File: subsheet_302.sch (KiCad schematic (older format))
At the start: 14 parts, among them J302 Internal FDD Power, J303 Internal FDD Port, J304 DIN-14S — External FDD Port, U301 WD1772_FLOPPY_DISK_CONTROLLER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, U305 7406_PHY

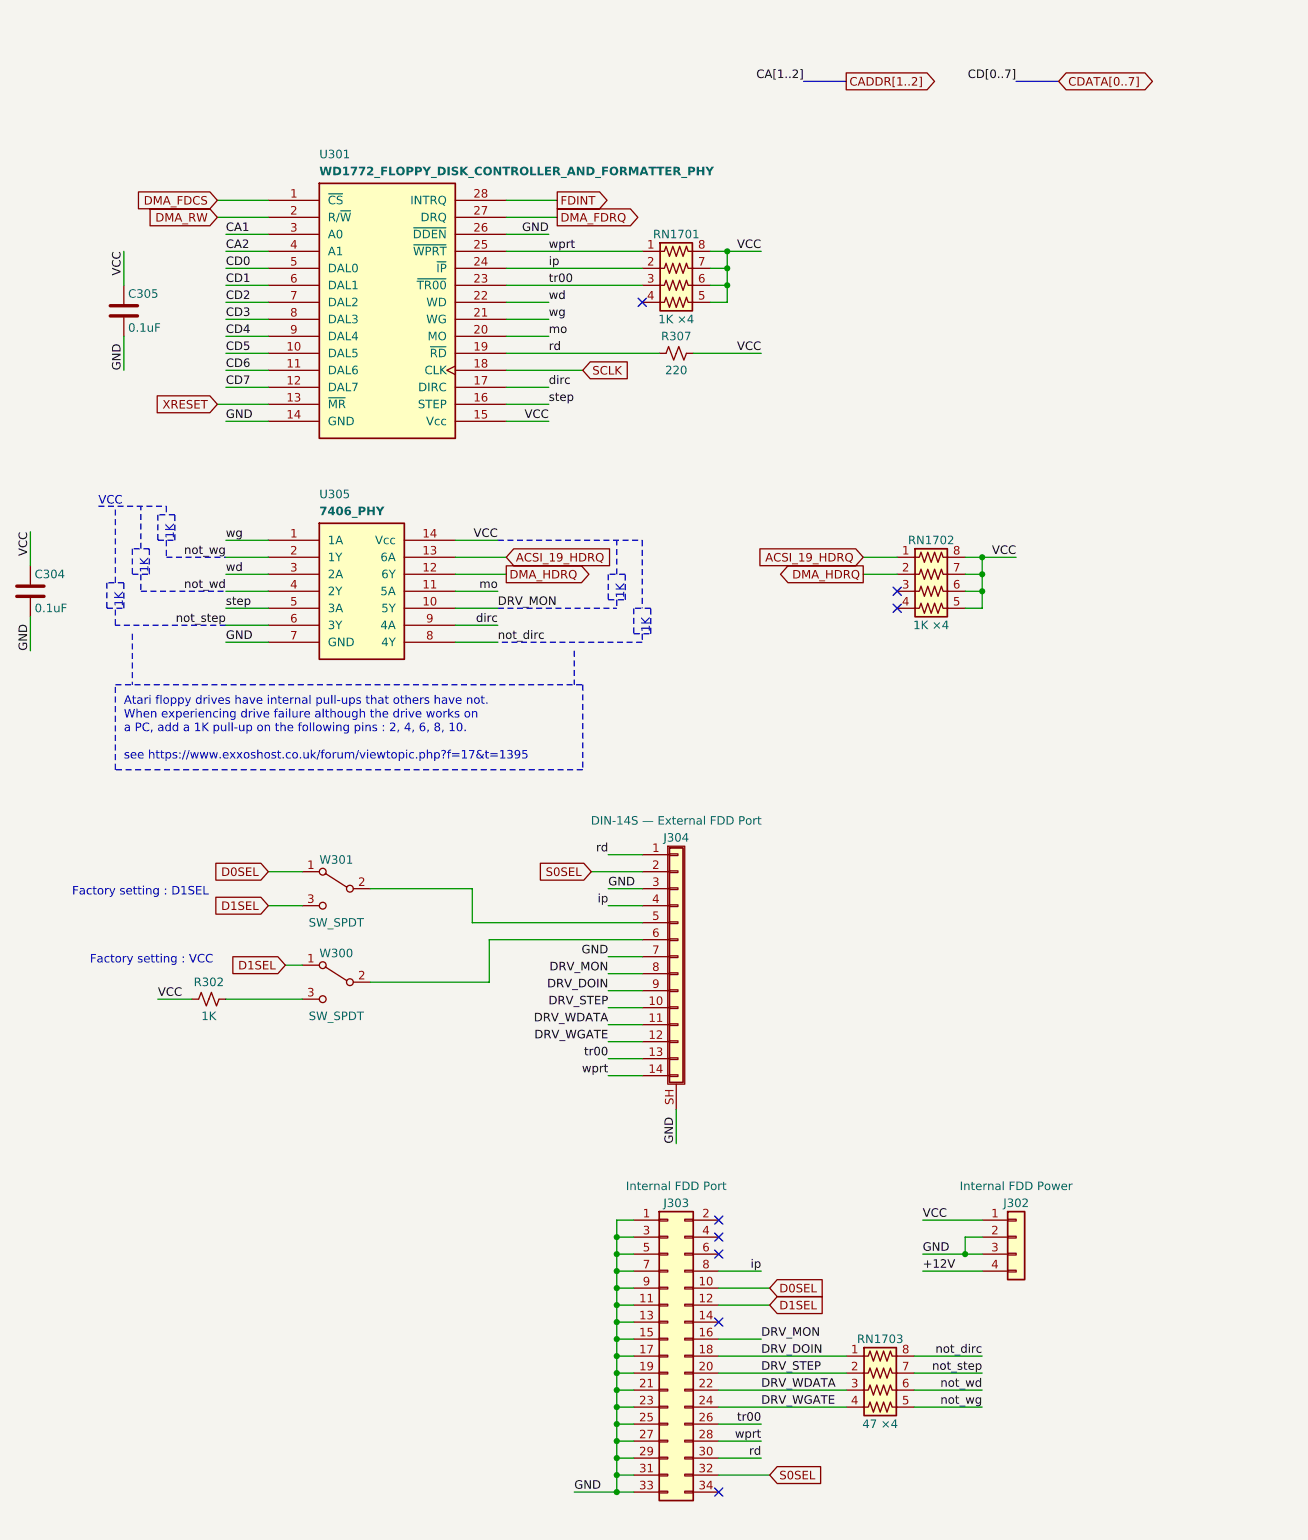
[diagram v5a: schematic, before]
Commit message: Resolves #4 : Apply the 1772 pull-up fix
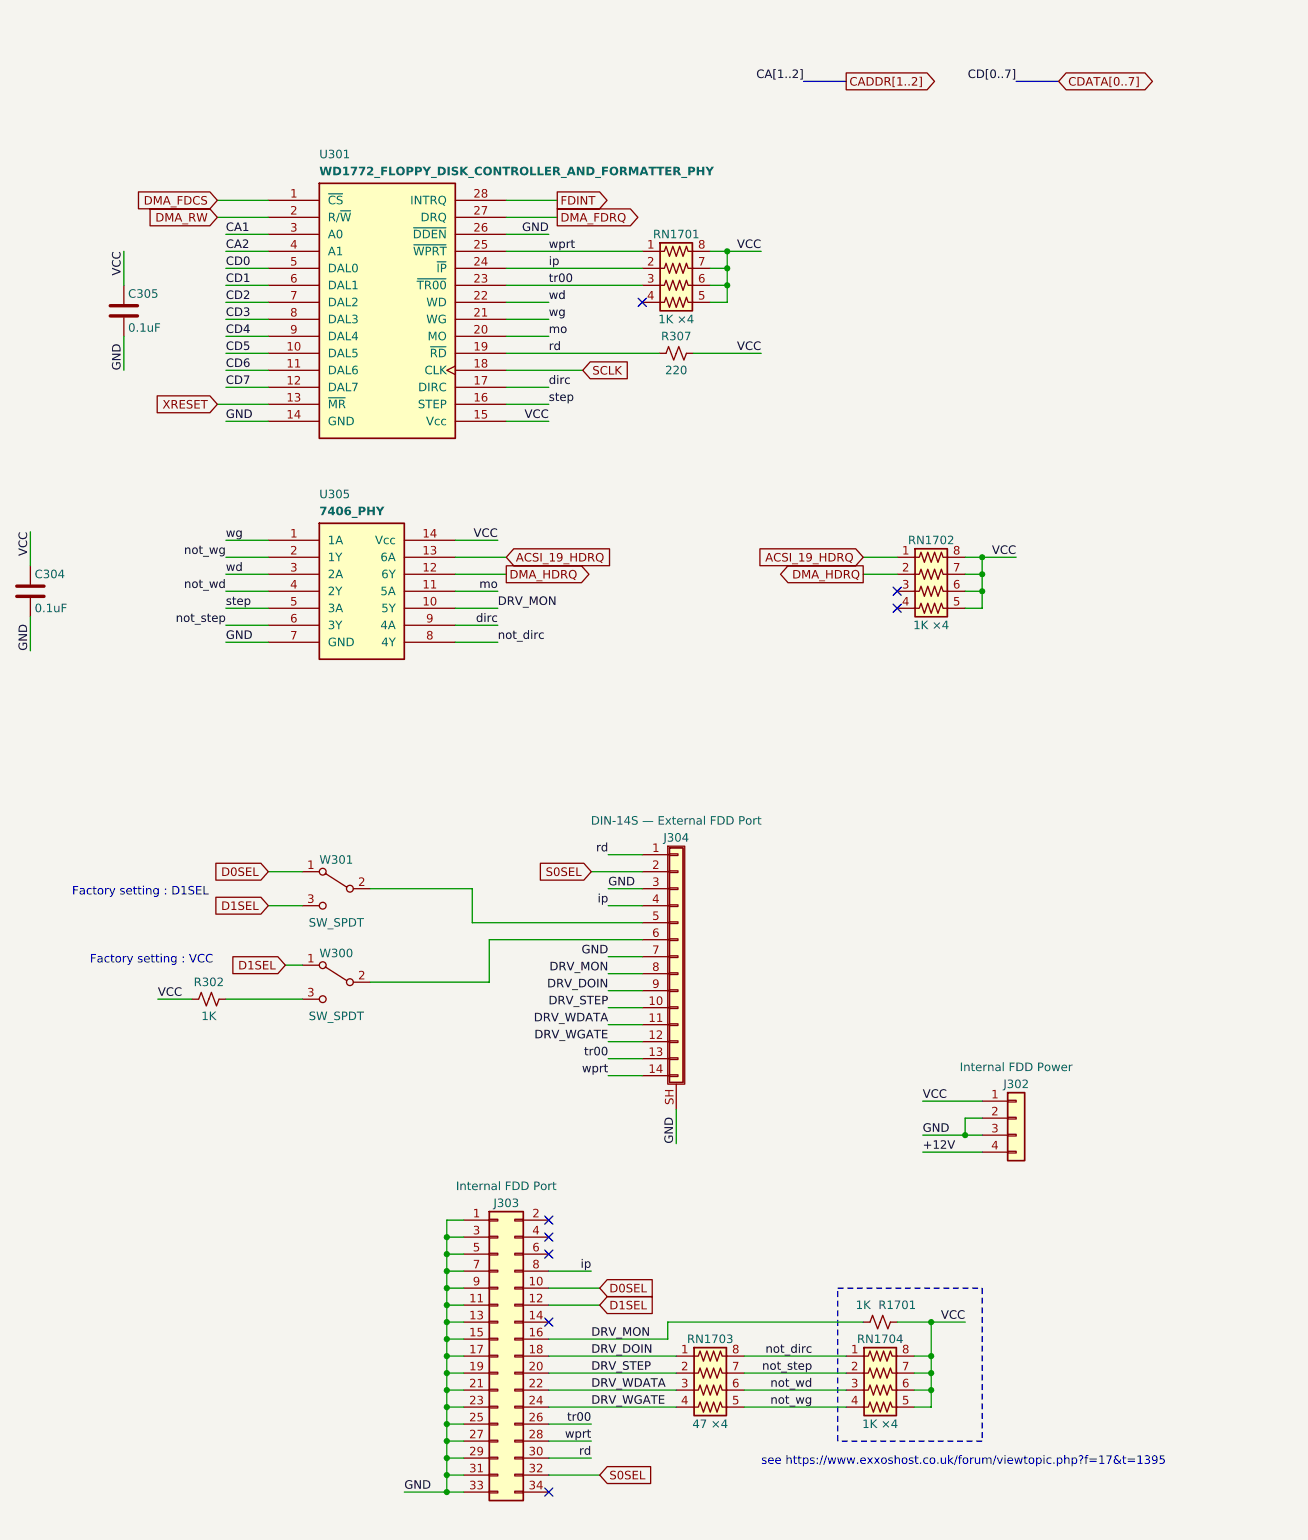
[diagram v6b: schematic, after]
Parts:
- added R1701: 1K, commons_passives_THT:Passive_THT_resistor_W2.54mm_L12.70mm, symbol Device:R_Small_US
- added RN1704: 1K ×4, Resistor_SMD:R_Array_Convex_4x0603, symbol custom_passives:R_Pack04_US
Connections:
- net DRV_MON: now also R1701.2
- net VCC: now also R1701.1, RN1704.5 (R4.2), RN1704.6 (R3.2), RN1704.7 (R2.2), RN1704.8 (R1.2)
- net not_dirc: now also RN1704.1 (R1.1)
- net not_step: now also RN1704.2 (R2.1)
- net not_wd: now also RN1704.3 (R3.1)
- net not_wg: now also RN1704.4 (R4.1)
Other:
- note added: "see https://www.exxoshost.co.uk/forum/viewtopic.php?f=17&t=1395"
- note removed: "1K"
- note removed: "Atari floppy drives have internal pull-ups that others have not.\nWhen experiencing drive failure although the drive works on\na PC, add a 1K pull-up on the following pins : 2, 4, 6, 8, 10.\n\nsee https://www.exxoshost.co.uk/forum/viewtopic.php?f=17&t=1395"
- note removed: "VCC"
- moved on the sheet: J302, J303, RN1703

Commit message: Resolves #13 : assign 1206 hand-solder footprints to resistors
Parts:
- R1701, R302, R307: footprint commons_passives_THT:Passive_THT_resistor_W2.54mm_L12.70mm -> Resistor_SMD:R_1206_3216Metric_Pad1.30x1.75mm_HandSolder
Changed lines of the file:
@@
 F 0 "R307" V 4400 2600 50  0000 C CNN
 F 1 "220" V 4600 2600 50  0000 C CNN
-F 2 "commons_passives_THT:Passive_THT_resistor_W2.54mm_L12.70mm" H 4500 2600 50  0001 C CNN
+F 2 "Resistor_SMD:R_1206_3216Metric_Pad1.30x1.75mm_HandSolder" H 4500 2600 50  0001 C CNN
 F 3 "~" H 4500 2600 50  0001 C CNN
 	1    4500 2600
@@
 F 0 "R302" V 1650 6400 50  0000 C CNN
 F 1 "1K" V 1850 6400 50  0000 C CNN
-F 2 "commons_passives_THT:Passive_THT_resistor_W2.54mm_L12.70mm" H 1750 6400 50  0001 C CNN
+F 2 "Resistor_SMD:R_1206_3216Metric_Pad1.30x1.75mm_HandSolder" H 1750 6400 50  0001 C CNN
 F 3 "~" H 1750 6400 50  0001 C CNN
 	1    1750 6400
@@
 F 0 "R1701" V 5600 8400 50  0000 C CNN
 F 1 "1K" V 5600 8200 50  0000 C CNN
-F 2 "commons_passives_THT:Passive_THT_resistor_W2.54mm_L12.70mm" H 5700 8300 50  0001 C CNN
+F 2 "Resistor_SMD:R_1206_3216Metric_Pad1.30x1.75mm_HandSolder" H 5700 8300 50  0001 C CNN
 F 3 "~" H 5700 8300 50  0001 C CNN
 	1    5700 8300
